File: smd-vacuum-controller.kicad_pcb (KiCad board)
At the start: 2 copper layers, 60 x 60 mm, 84 parts, among them J1 ST-LINK, J2 UART_BOOT, J3 USB, J4 Conn_01x02, J5 Conn_01x02, J6 Barrel_Jack_Switch, J7 ST-LINKV2, J8 UART_BOOT, Q1 MMBT3904, Q2 IRF3205, Q3 MMBT3904, Q4 MMBT3904, Q5 MMBT3904, Q6 MMBT3904, SW1 SW_Push, SW2 BTN_RST, SW3 BTN_BOOT, U1 STM32F103C8Tx, U2 USBLC6-2SC6, U3 TD6811, U4 DRV8876RGTR, U5 TD6811, Y1 8MHz

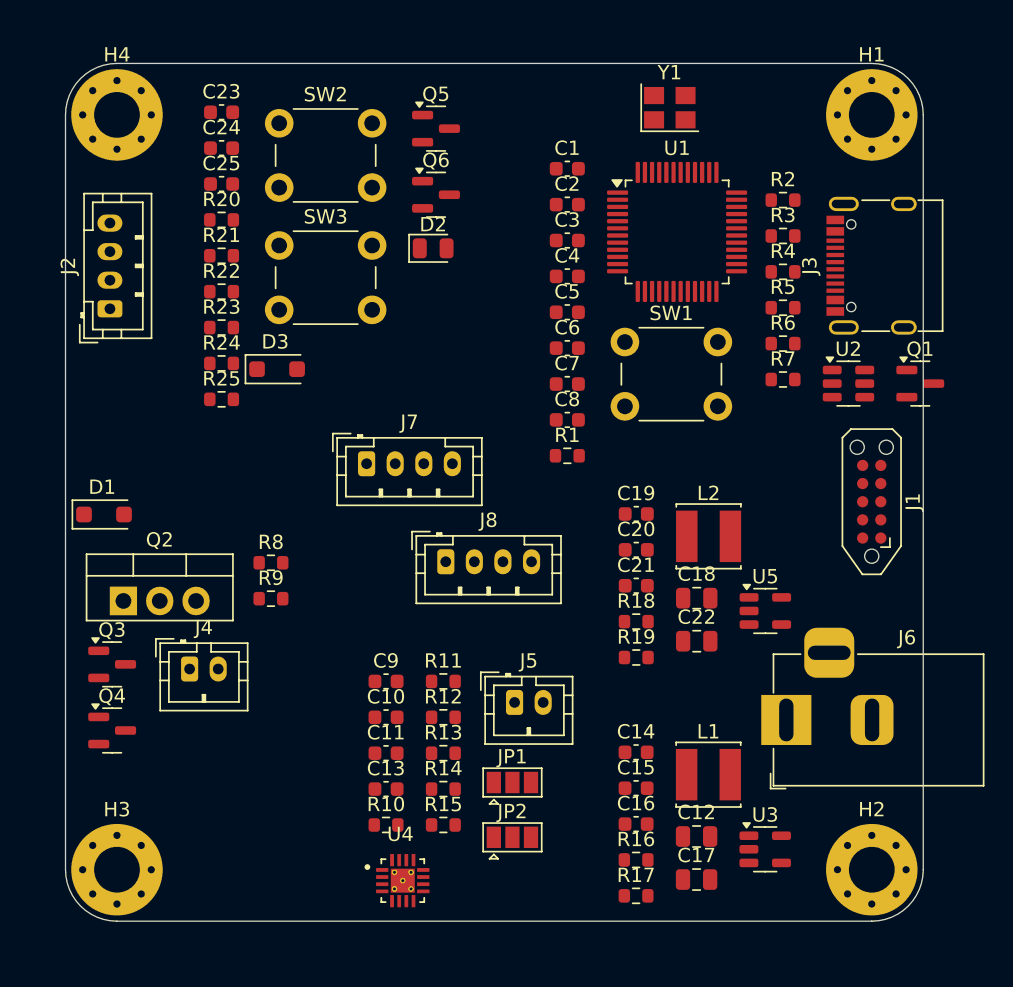
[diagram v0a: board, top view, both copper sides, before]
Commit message: Added footwitch, usb led activity
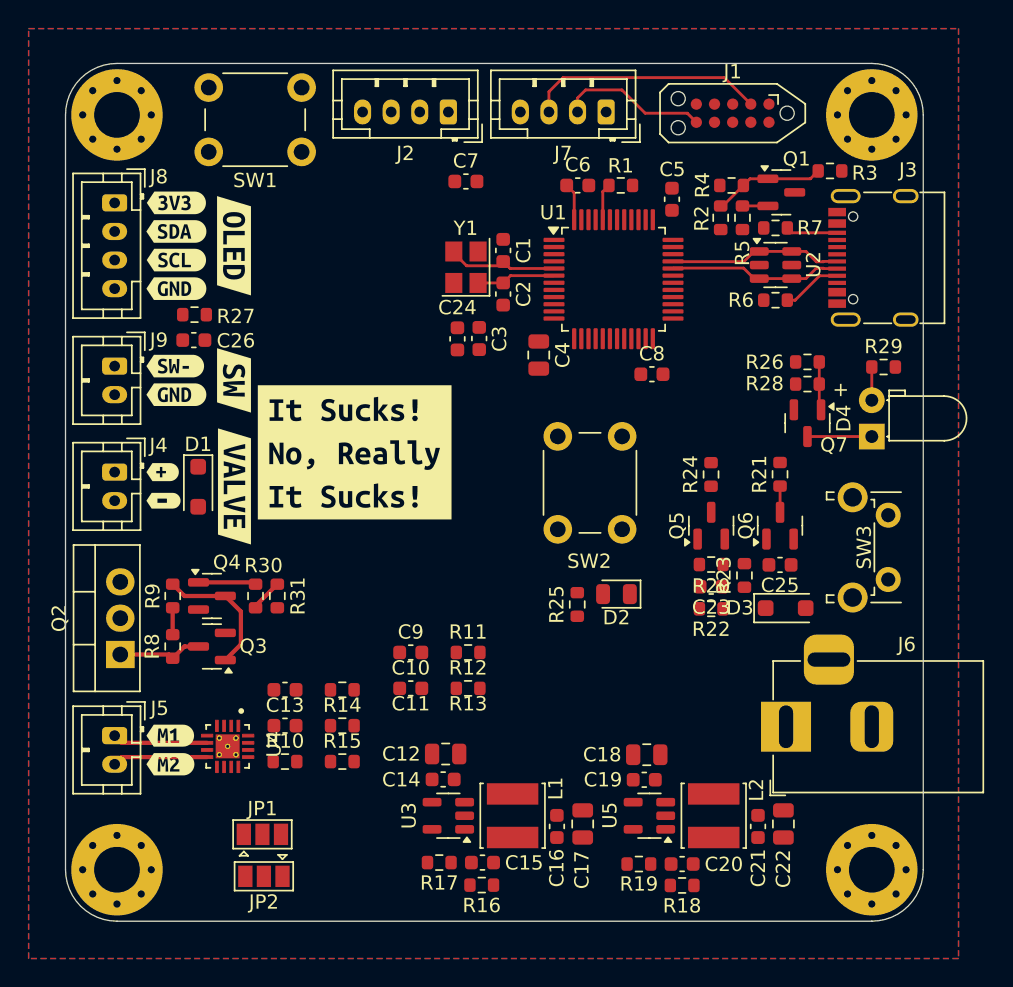
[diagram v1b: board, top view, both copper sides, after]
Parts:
- added C26: 100nF, Capacitor_SMD:C_0603_1608Metric, F.Cu at (97.0, 86.6)
- added D4: LED, LED_THT:LED_D3.0mm_Horizontal_O1.27mm_Z2.0mm, F.Cu at (144.4, 93.4)
- added J9: Conn_01x02, Connector_JST:JST_PH_B2B-PH-K_1x02_P2.00mm_Vertical, F.Cu at (91.5, 88.5)
- added Q7: MMBT3904, Package_TO_SOT_SMD:SOT-23, F.Cu at (139.9, 92.4)
- added R26: 100R, Resistor_SMD:R_0603_1608Metric, F.Cu at (139.9, 88.2)
- added R27: 100K, Resistor_SMD:R_0603_1608Metric, F.Cu at (97.1, 84.9)
- added R28: 10K, Resistor_SMD:R_0603_1608Metric, F.Cu at (139.9, 89.7)
- added R29: 1.5K, Resistor_SMD:R_0603_1608Metric, F.Cu at (145.3, 88.5)
- added R30: 1K, Resistor_SMD:R_0603_1608Metric, F.Cu at (101.3, 104.5)
- added R31: 10K, Resistor_SMD:R_0603_1608Metric, F.Cu at (102.8, 104.5)
- added kibuzzard-68A6E781: G***, kibuzzard-68A6E781, F.Cu at (95.8, 79.0)
- added kibuzzard-68A6E791: G***, kibuzzard-68A6E791, F.Cu at (95.8, 77.0)
- added kibuzzard-68A6E799: G***, kibuzzard-68A6E799, F.Cu at (95.8, 83.0)
- added kibuzzard-68A6E799: G***, kibuzzard-68A6E799, F.Cu at (95.8, 90.5)
- added kibuzzard-68A6E7A0: G***, kibuzzard-68A6E7A0, F.Cu at (95.8, 81.0)
- added kibuzzard-68A6E7E9: G***, kibuzzard-68A6E7E9, F.Cu at (95.7, 88.5)
- added kibuzzard-68A6E83D: G***, kibuzzard-68A6E83D, F.Cu at (94.8, 95.9)
- added kibuzzard-68A6E857: G***, kibuzzard-68A6E857, F.Cu at (94.9, 97.9)
- added kibuzzard-68A6E8E7: G***, kibuzzard-68A6E8E7, F.Cu at (95.4, 114.3)
- added kibuzzard-68A6E8EF: G***, kibuzzard-68A6E8EF, F.Cu at (95.4, 116.3)
- added kibuzzard-68A6EB23: G***, kibuzzard-68A6EB23, F.Cu at (99.8, 80.0)
- added kibuzzard-68A6EB93: G***, kibuzzard-68A6EB93, F.Cu at (99.8, 89.5)
- added kibuzzard-68A6EBD4: G***, kibuzzard-68A6EBD4, F.Cu at (99.8, 96.9)
- added kibuzzard-68A6ED99: G***, kibuzzard-68A6ED99, F.Cu at (108.3, 94.5)
- C4: footprint Capacitor_SMD:C_0603_1608Metric -> Capacitor_SMD:C_0805_2012Metric
- SW3: footprint Button_Switch_THT:SW_PUSH_6mm_H5mm -> Button_Switch_THT:SW_Tactile_SPST_Angled_PTS645Vx83-2LFS
- moved C23 47.7 mm to (133.2, 103.9), turned to 180 degrees
- moved C25 47.3 mm to (138.0, 102.4), turned to 180 degrees
- moved SW3 46.6 mm to (145.6, 98.9), turned to -90 degrees
- moved R21 41.9 mm to (138.0, 96.0), turned to 90 degrees
- moved R20 41.9 mm to (133.2, 102.3)
- moved R22 40.8 mm to (133.2, 105.4), turned to 180 degrees
- moved R23 40.5 mm to (135.5, 103.1), turned to 90 degrees
- moved D3 39.3 mm to (138.4, 105.4)
- moved R24 35.1 mm to (133.2, 96.0), turned to 90 degrees
- moved SW2 34.4 mm to (122.5, 99.9), turned to 90 degrees
- moved J8 34.2 mm to (91.5, 77.0), turned to -90 degrees
- moved Q5 33.8 mm to (133.2, 99.6), turned to 90 degrees
- moved Q6 33.4 mm to (138.0, 99.6), turned to 90 degrees
- moved J7 29.8 mm to (125.8, 70.7), turned to 180 degrees
- moved J1 28.9 mm to (134.7, 70.8), turned to 180 degrees
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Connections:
- C24 pad 2: /USB/RESET -> /MCU/NRST
- J3 pad A6: /USB/USB_D+ -> /MCU/USB_D+
- J3 pad A7: /USB/USB_D- -> /MCU/USB_D-
- J3 pad B6: /USB/USB_D+ -> /MCU/USB_D+
- J3 pad B7: /USB/USB_D- -> /MCU/USB_D-
- J7 pad 1: VMCU -> GND
- J7 pad 2: /MCU/SWDIO -> /MCU/SWCLK
- J7 pad 3: /MCU/SWCLK -> /MCU/SWDIO
- J7 pad 4: GND -> VMCU
- Q4 pad 1: /MOSFET/SOLENOID -> Net-(Q4-B)
- Q5 pad 3: /USB/RESET -> /MCU/NRST
- R1 pad 2: VMCU -> /MCU/BOOT0
- R24 pad 1: /USB/RESET -> /MCU/NRST
- R5 pad 1: /USB/USB_D+ -> /MCU/USB_D+
- SW1 pad 1: GND -> /MCU/BOOT0
- SW2 pad 2: /USB/RESET -> /MCU/NRST
- SW3 pad 1: Net-(D3-A) -> VMCU
- SW3 pad 2: VMCU -> Net-(D3-A)
- U1 pad 44: VMCU -> /MCU/BOOT0
- U2 pad 1: /USB/USB_D+ -> /MCU/USB_D+
- U2 pad 3: /USB/USB_D- -> /MCU/USB_D-
- U2 pad 4: /USB/USB_D- -> /MCU/USB_D-
- U2 pad 6: /USB/USB_D+ -> /MCU/USB_D+
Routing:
- net /MCU/SWDIO: track 0.00 -> 16.7 mm
- net /MCU/USB_D-: track 0.00 -> 12.1 mm
- net /MCU/USB_D+: track 0.00 -> 12.1 mm
- net /MCU/SWCLK: track 0.00 -> 10.5 mm
- net Net-(Q3-B): track 0.00 -> 9.40 mm
- net Net-(Q1-B): track 0.00 -> 7.84 mm
- net Net-(U1-PD0): track 0.00 -> 7.81 mm
- net Net-(J5-Pin_2): track 0.00 -> 6.68 mm
- net Net-(J5-Pin_1): track 0.00 -> 6.68 mm
- net Net-(Q2-G): track 0.00 -> 5.92 mm
- net Net-(U1-PD1): track 0.00 -> 5.52 mm
- net Net-(D4-K): track 0.00 -> 4.50 mm
- net Net-(J3-CC1): track 0.00 -> 4.19 mm
- net Net-(Q4-B): track 0.00 -> 4.04 mm
- net Net-(J3-CC2): track 0.00 -> 3.63 mm
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- added copper zone on B.Cu, net GND
- added copper zone on F.Cu, net GND
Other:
- board text added: "+"

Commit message: layouting Power, Motor section
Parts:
- added R32: 2.2K, Resistor_SMD:R_0603_1608Metric, F.Cu at (101.9, 78.7)
- added R33: 2.2K, Resistor_SMD:R_0603_1608Metric, F.Cu at (103.5, 78.7)
- added TP1: TestPoint, TestPoint:TestPoint_Pad_D1.0mm, F.Cu at (138.4, 121.3)
- added TP2: TestPoint, TestPoint:TestPoint_Pad_D1.0mm, F.Cu at (133.0, 109.6)
- added TP3: TestPoint, TestPoint:TestPoint_Pad_D1.0mm, F.Cu at (131.3, 126.0)
- added TP4: TestPoint, TestPoint:TestPoint_Pad_D1.0mm, F.Cu at (118.0, 126.0)
- added kibuzzard-68A6E791: G***, kibuzzard-68A6E791, F.Cu at (114.8, 74.9)
- added kibuzzard-68A6E791: G***, kibuzzard-68A6E791, F.Cu at (119.8, 74.9)
- added kibuzzard-68A6E799: G***, kibuzzard-68A6E799, F.Cu at (125.8, 75.0)
- added kibuzzard-68A6E799: G***, kibuzzard-68A6E799, F.Cu at (108.8, 75.0)
- added kibuzzard-68A7C4E3: G***, kibuzzard-68A7C4E3, F.Cu at (106.3, 120.4)
- added kibuzzard-68A7C639: G***, kibuzzard-68A7C639, F.Cu at (112.8, 74.5)
- added kibuzzard-68A7C63E: G***, kibuzzard-68A7C63E, F.Cu at (110.8, 74.5)
- added kibuzzard-68A7C6B4: G***, kibuzzard-68A7C6B4, F.Cu at (111.8, 78.4)
- added kibuzzard-68A7C770: G***, kibuzzard-68A7C770, F.Cu at (121.8, 74.9)
- added kibuzzard-68A7C776: G***, kibuzzard-68A7C776, F.Cu at (123.8, 75.0)
- added kibuzzard-68A7C7AA: G***, kibuzzard-68A7C7AA, F.Cu at (119.1, 78.4)
- added kibuzzard-68A7C961: G***, kibuzzard-68A7C961, F.Cu at (101.4, 75.9)
- added kibuzzard-68A7C9BE: G***, kibuzzard-68A7C9BE, F.Cu at (121.5, 95.1)
- C9: footprint Capacitor_SMD:C_0603_1608Metric -> Capacitor_THT:CP_Radial_D6.3mm_P2.50mm
- moved C22 25.7 mm to (112.8, 123.8)
- moved C21 22.1 mm to (114.6, 123.6)
- moved R25 21.5 mm to (139.8, 90.8), turned to 180 degrees
- moved C12 21.1 mm to (135.6, 118.0), turned to -90 degrees
- moved C14 19.4 mm to (133.8, 117.8), turned to 90 degrees
- moved C9 18.9 mm to (99.0, 122.1), turned to -90 degrees
- moved R18 18.6 mm to (113.1, 120.4), turned to 90 degrees
- moved C10 18.0 mm to (95.6, 117.9), turned to 180 degrees
- moved C20 16.8 mm to (114.6, 120.5), turned to -90 degrees
- moved D2 16.7 mm to (136.3, 90.9), turned to 0 degrees
- moved U3 16.6 mm to (131.3, 118.2), turned to 90 degrees
- moved R26 15.9 mm to (137.9, 103.9), turned to 0 degrees
- moved L2 15.7 mm to (118.0, 122.7), turned to 180 degrees
- moved R17 15.0 mm to (128.0, 117.5), turned to 90 degrees
- moved R19 14.8 mm to (114.6, 117.4), turned to 90 degrees
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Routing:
- net VIN: track 0.00 -> 31.7 mm
- net VSOLENOID: track 1.88 -> 30.7 mm
- net VMCU: track 2.62 -> 27.7 mm
- net Net-(D3-A): track 0.00 -> 21.1 mm
- net Net-(D1-A): track 0.00 -> 15.9 mm
- net /MCU/OLED_SCL: track 0.00 -> 12.6 mm
- net /MCU/OLED_SDA: track 0.00 -> 10.7 mm
- net VMOTOR: track 0.00 -> 8.62 mm
- net /MCU/FOOTSW: track 0.00 -> 7.30 mm
- net Net-(D4-K): track 4.50 -> 10.9 mm
- net Net-(U3-FB): track 0.00 -> 5.92 mm
- net Net-(U5-FB): track 0.00 -> 5.90 mm
- net /MCU/USB_D+: track 12.1 -> 17.1 mm
- net Net-(Q5-B): track 0.00 -> 4.88 mm
- net Net-(D3-K): track 0.00 -> 4.20 mm
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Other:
- board text added: "-"
- board text added: "V-MCU"
- board text added: "V-VALVE"

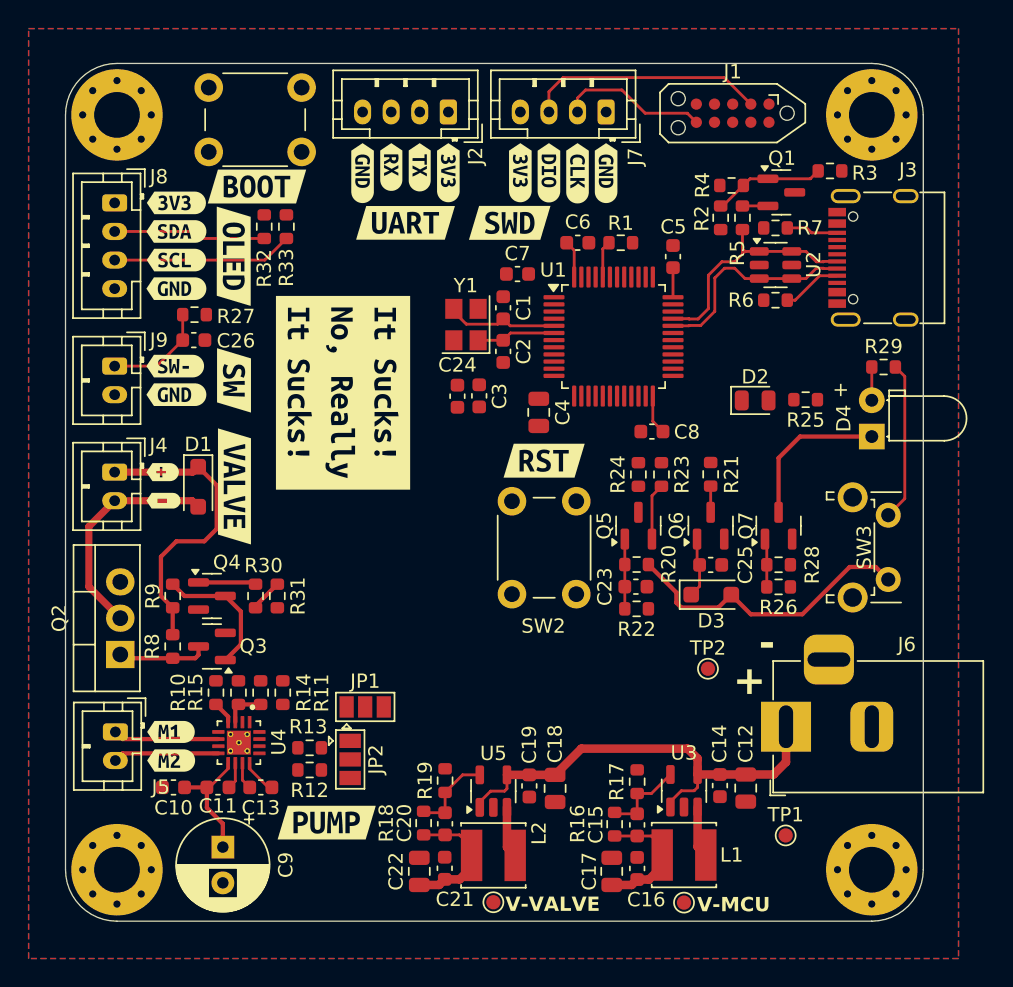
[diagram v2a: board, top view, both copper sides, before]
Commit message: Added push button connector
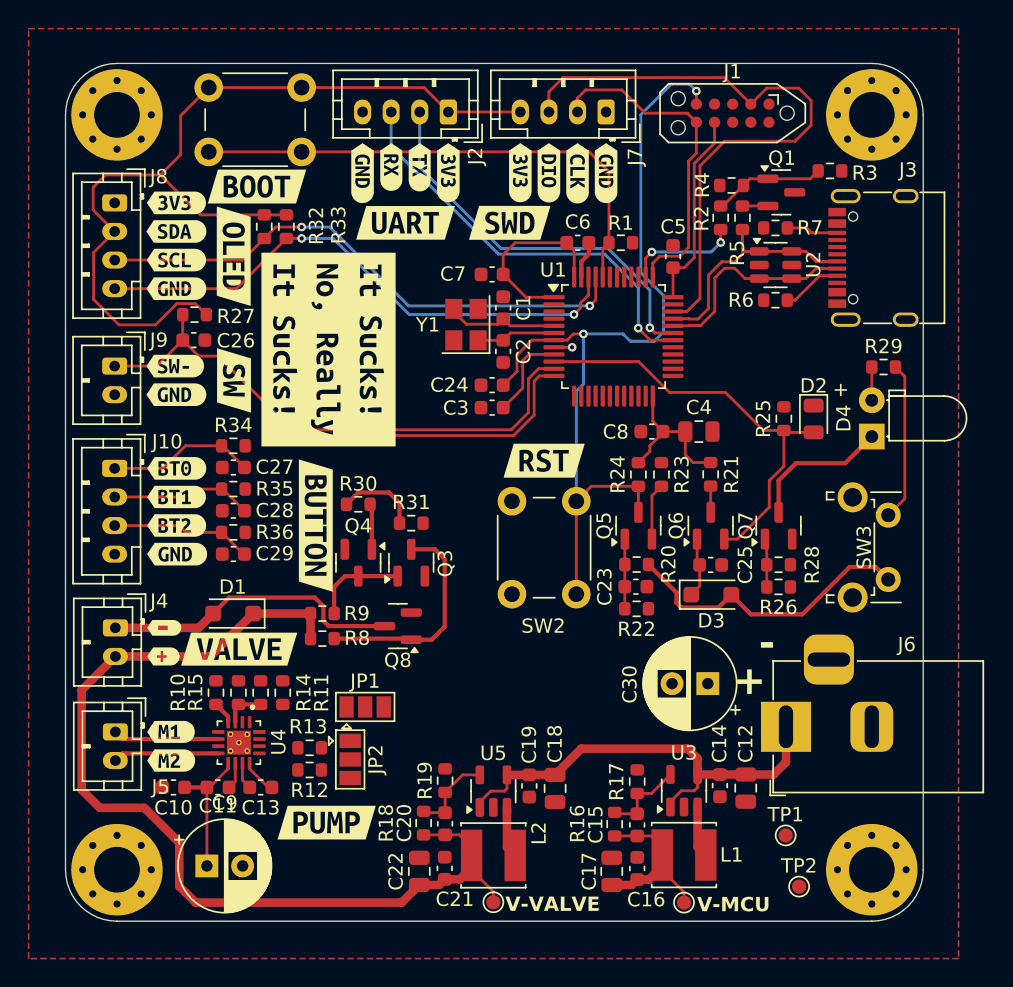
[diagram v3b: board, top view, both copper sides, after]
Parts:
- removed Q2: IRF3205, Package_TO_SOT_THT:TO-220-3_Vertical
- removed kibuzzard-68A6EB23: G***, kibuzzard-68A6EB23
- removed kibuzzard-68A6EB93: G***, kibuzzard-68A6EB93
- removed kibuzzard-68A6EBD4: G***, kibuzzard-68A6EBD4
- removed kibuzzard-68A7C4E3: G***, kibuzzard-68A7C4E3
- removed kibuzzard-68A7C6B4: G***, kibuzzard-68A7C6B4
- removed kibuzzard-68A7C7AA: G***, kibuzzard-68A7C7AA
- removed kibuzzard-68A7C961: G***, kibuzzard-68A7C961
- removed kibuzzard-68A7C9BE: G***, kibuzzard-68A7C9BE
- added C27: 100nF, Capacitor_SMD:C_0603_1608Metric, F.Cu at (99.8, 95.5)
- added C28: 100nF, Capacitor_SMD:C_0603_1608Metric, F.Cu at (99.8, 98.6)
- added C29: 100nF, Capacitor_SMD:C_0603_1608Metric, F.Cu at (99.8, 101.6)
- added C30: 220uF, Capacitor_THT:CP_Radial_D6.3mm_P2.50mm, F.Cu at (133.0, 110.7)
- added J10: UI_BTN, Connector_JST:JST_PH_B4B-PH-K_1x04_P2.00mm_Vertical, F.Cu at (91.5, 95.6)
- added Q8: AO3400A, Package_TO_SOT_SMD:SOT-23, F.Cu at (111.3, 106.6)
- added R34: 100K, Resistor_SMD:R_0603_1608Metric, F.Cu at (99.8, 94.0)
- added R35: 100K, Resistor_SMD:R_0603_1608Metric, F.Cu at (99.8, 97.1)
- added R36: 100K, Resistor_SMD:R_0603_1608Metric, F.Cu at (99.8, 100.1)
- added kibuzzard-68A6E799: G***, kibuzzard-68A6E799, F.Cu at (95.8, 101.6)
- added kibuzzard-68AA9AC7: G***, kibuzzard-68AA9AC7, F.Cu at (95.8, 95.6)
- added kibuzzard-68AA9ACD: G***, kibuzzard-68AA9ACD, F.Cu at (95.8, 97.6)
- added kibuzzard-68AA9AD3: G***, kibuzzard-68AA9AD3, F.Cu at (95.8, 99.6)
- added kibuzzard-68AA9F08: G***, kibuzzard-68AA9F08, F.Cu at (100.2, 108.3)
- added kibuzzard-68AA9F21: G***, kibuzzard-68AA9F21, F.Cu at (105.5, 99.6)
- added kibuzzard-68AA9F28: G***, kibuzzard-68AA9F28, F.Cu at (99.8, 89.5)
- added kibuzzard-68AA9F3B: G***, kibuzzard-68AA9F3B, F.Cu at (111.8, 78.4)
- added kibuzzard-68AA9F3F: G***, kibuzzard-68AA9F3F, F.Cu at (101.4, 75.9)
- added kibuzzard-68AA9F46: G***, kibuzzard-68AA9F46, F.Cu at (99.8, 80.8)
- added kibuzzard-68AA9F51: G***, kibuzzard-68AA9F51, F.Cu at (119.1, 78.4)
- added kibuzzard-68AA9F57: G***, kibuzzard-68AA9F57, F.Cu at (121.5, 95.1)
- added kibuzzard-68AA9F5E: G***, kibuzzard-68AA9F5E, F.Cu at (106.3, 120.4)
- moved TP2 16.5 mm to (139.3, 124.9)
- moved Q3 15.1 mm to (112.2, 102.2), turned to 90 degrees
- moved kibuzzard-68A6E83D 12.9 mm to (94.9, 108.8)
- moved C4 11.3 mm to (132.3, 93.0), turned to 0 degrees
- moved J4 10.9 mm to (91.5, 106.8)
- moved R31 10.7 mm to (112.2, 99.4), turned to 180 degrees
- moved R9 10.5 mm to (106.0, 105.8), turned to 180 degrees
- moved Q4 10.5 mm to (108.5, 102.2), turned to -90 degrees
- moved R8 10.5 mm to (106.0, 107.5), turned to 180 degrees
- moved R30 9.64 mm to (108.5, 98.1), turned to 180 degrees
- moved D1 9.20 mm to (99.7, 105.8), turned to 180 degrees
- moved kibuzzard-68A6E857 8.89 mm to (94.9, 106.8)
- moved D2 4.29 mm to (140.4, 92.2), turned to -90 degrees
- moved kibuzzard-68A6ED99 3.19 mm to (106.4, 87.3)
- moved C24 2.55 mm to (117.9, 89.8), turned to 0 degrees
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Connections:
- D2 pad 2: /USB/SOFT_BOOT -> /MCU/SOFT_BOOT
- J2 pad 2: /MCU/UART_TX -> /MCU/USART1_RX
- J2 pad 3: /MCU/UART_RX -> /MCU/USART1_TX
- J4 pad 1: VSOLENOID -> Net-(D1-A)
- J4 pad 2: Net-(D1-A) -> VSOLENOID
- J8 pad 1: VMCU -> GND
- J8 pad 2: /MCU/OLED_SDA -> VMCU
- J8 pad 4: GND -> /MCU/OLED_SDA
- Q6 pad 2: /USB/SOFT_BOOT -> /MCU/SOFT_BOOT
- R25 pad 2: /USB/SOFT_BOOT -> /MCU/SOFT_BOOT
- R32 pad 1: /MCU/OLED_SDA -> /MCU/OLED_SCL
- R33 pad 1: /MCU/OLED_SCL -> /MCU/OLED_SDA
- U1 pad 10: unconnected-(U1-PA0-Pad10) -> /MCU/SOFT_BOOT
- U1 pad 11: unconnected-(U1-PA1-Pad11) -> /MCU/FOOTSW
- U1 pad 12: unconnected-(U1-PA2-Pad12) -> /MOSFET/SOLENOID
- U1 pad 30: unconnected-(U1-PA9-Pad30) -> /MCU/USART1_TX
- U1 pad 31: unconnected-(U1-PA10-Pad31) -> /MCU/USART1_RX
- U1 pad 38: unconnected-(U1-PA15-Pad38) -> /USB/USB_RENUM
- U1 pad 45: unconnected-(U1-PB8-Pad45) -> /MCU/OLED_SCL
- U1 pad 46: unconnected-(U1-PB9-Pad46) -> /MCU/OLED_SDA
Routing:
- net VMCU: track 27.7 -> 131.8 mm
- net /MCU/NRST: track 0.00 -> 60.6 mm, vias 0 -> 2
- net VSOLENOID: track 30.7 -> 69.3 mm
- net /MCU/BOOT0: track 2.58 -> 36.1 mm
- net /MCU/FOOTSW: track 7.30 -> 39.0 mm
- net /MCU/SOFT_BOOT: track 0.00 -> 30.1 mm
- net /MCU/USART1_TX: track 0.00 -> 29.4 mm, vias 0 -> 1
- net /MCU/OLED_SDA: track 10.7 -> 38.8 mm, vias 0 -> 2
- net /MCU/USART1_RX: track 0.00 -> 27.9 mm, vias 0 -> 1
- net /MCU/SWDIO: track 16.7 -> 44.0 mm
- net /MCU/OLED_SCL: track 12.6 -> 38.7 mm, vias 0 -> 2
- net /MOSFET/SOLENOID: track 2.28 -> 27.3 mm
- net /MCU/SWCLK: track 10.5 -> 23.4 mm
- net /MCU/BTN_0: track 0.00 -> 10.4 mm
- net /MCU/BTN_1: track 0.00 -> 9.94 mm
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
